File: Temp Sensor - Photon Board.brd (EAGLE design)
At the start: 43.8 x 52.7 mm, 16 parts

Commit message: Added Temp Sensor gerber files.  General cleanup or bck files
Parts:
- U$15: value 50 -> 100
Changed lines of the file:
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@@
 <layer number="21" name="tPlace" color="7" fill="1" visible="yes" active="yes"/>
 <layer number="22" name="bPlace" color="7" fill="1" visible="yes" active="yes"/>
-<layer number="23" name="tOrigins" color="15" fill="1" visible="yes" active="yes"/>
-<layer number="24" name="bOrigins" color="15" fill="1" visible="yes" active="yes"/>
+<layer number="23" name="tOrigins" color="15" fill="1" visible="no" active="yes"/>
+<layer number="24" name="bOrigins" color="15" fill="1" visible="no" active="yes"/>
 <layer number="25" name="tNames" color="7" fill="1" visible="yes" active="yes"/>
 <layer number="26" name="bNames" color="7" fill="1" visible="yes" active="yes"/>
@@
 <text x="60.325" y="99.3775" size="0.508" layer="27" align="center">9V</text>
 <text x="58.42" y="99.3775" size="0.508" layer="27" rot="R180" align="center">GND</text>
-<text x="56.1975" y="93.345" size="0.8128" layer="25" rot="R90">9V Power In</text>
-<text x="63.1825" y="47.9425" size="0.7112" layer="25" rot="R90">Temp Sensor Conn</text>
-<text x="87.3125" y="61.2775" size="1.27" layer="25" rot="R90">Wifi Temperature Sensor Control Board</text>
-<text x="87.3125" y="92.71" size="0.6096" layer="25" rot="R90">v1.0</text>
-<text x="83.185" y="48.5775" size="0.8128" layer="25" rot="R180">http://quiller.io</text>
+<text x="56.1975" y="93.345" size="0.6096" layer="25" rot="R90">9V Power In</text>
+<text x="63.1825" y="47.9425" size="0.6096" layer="25" rot="R90">Temp Sensor Conn</text>
+<text x="87.3125" y="61.2775" size="1" layer="25" rot="R90">Wifi Temperature Sensor Control Board</text>
+<text x="87.6725" y="89.19" size="0.6096" layer="25" rot="R90">v1.0</text>
+<text x="60.285" y="48.6775" size="0.8128" layer="25" rot="R180">http://quiller.io</text>
 <rectangle x1="52.64" y1="70.24" x2="54.64" y2="79.68" layer="16"/>
 <text x="53.3" y="74.82" size="0.3048" layer="27">680</text>
@@
 <element name="U$1" library="myhvac" package="JST_PH-2" value="" x="59.3725" y="92.71" rot="R180"/>
 <element name="D1" library="myhvac" package="LED-RGB-THR" value="LED-RGB-CC-THRU" x="47.38" y="59.37" rot="R90"/>
-<element name="U$15" library="myhvac" package="R0805" value="50" x="57.06" y="64.3" smashed="yes"/>
+<element name="U$15" library="myhvac" package="R0805" value="100" x="57.06" y="64.3" smashed="yes"/>
 <element name="U$16" library="myhvac" package="R0805" value="100" x="57.1" y="61.38" smashed="yes"/>
 <element name="U$17" library="myhvac" package="R0805" value="100" x="57.1" y="58.42" smashed="yes"/>

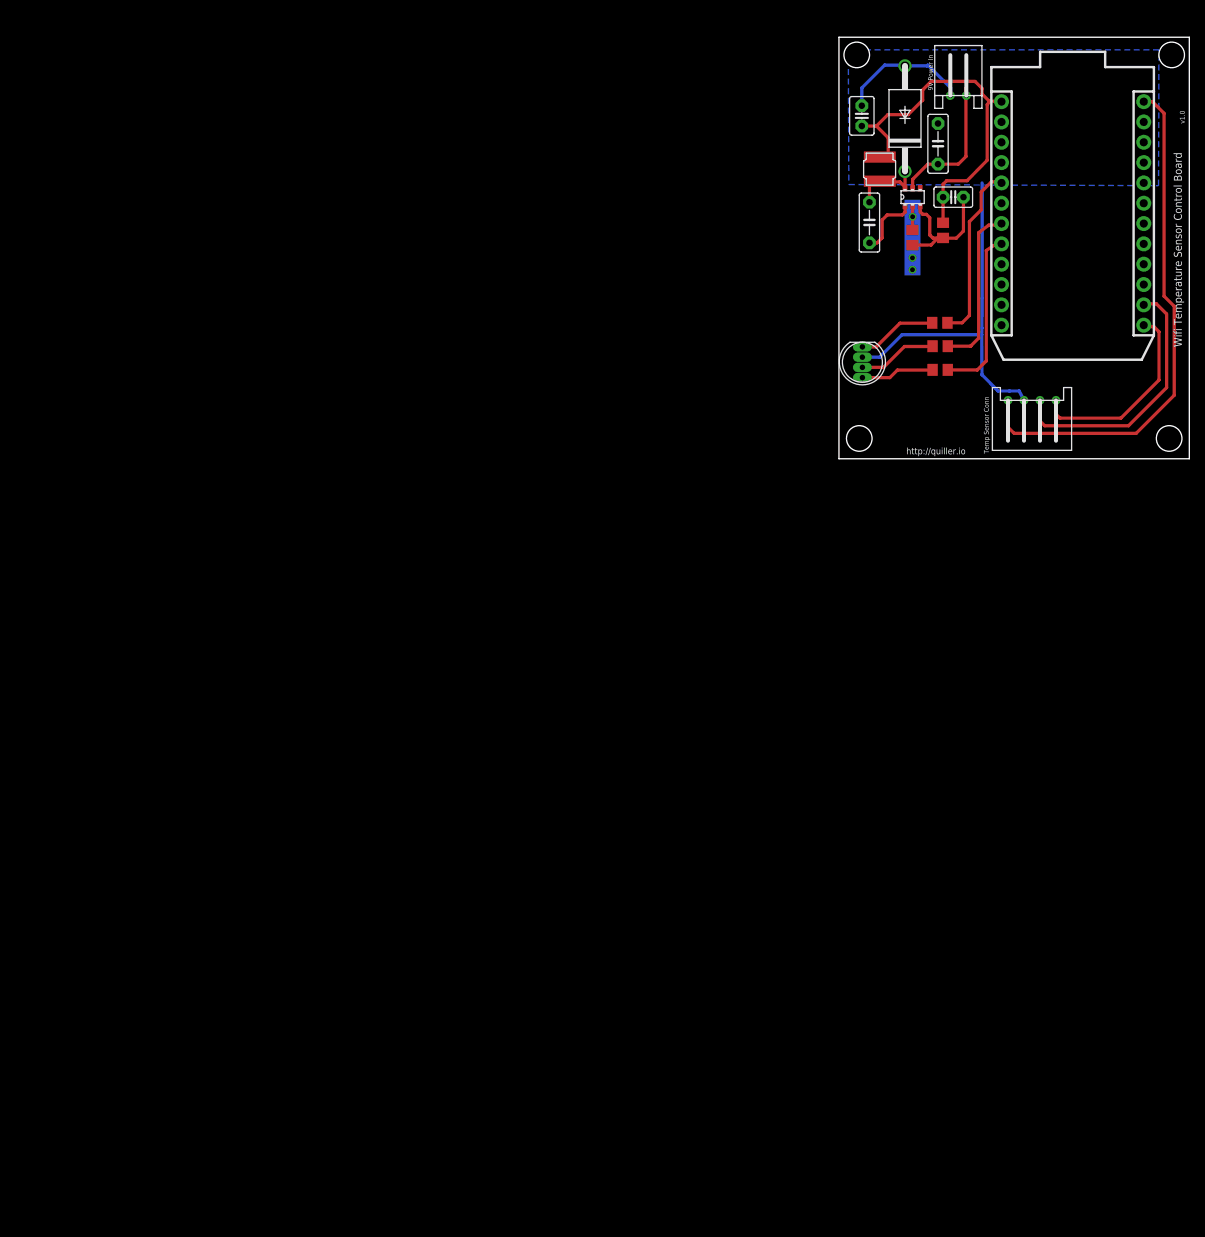
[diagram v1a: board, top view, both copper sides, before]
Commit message: Modified the temp sensor to use a prebuilt power converter
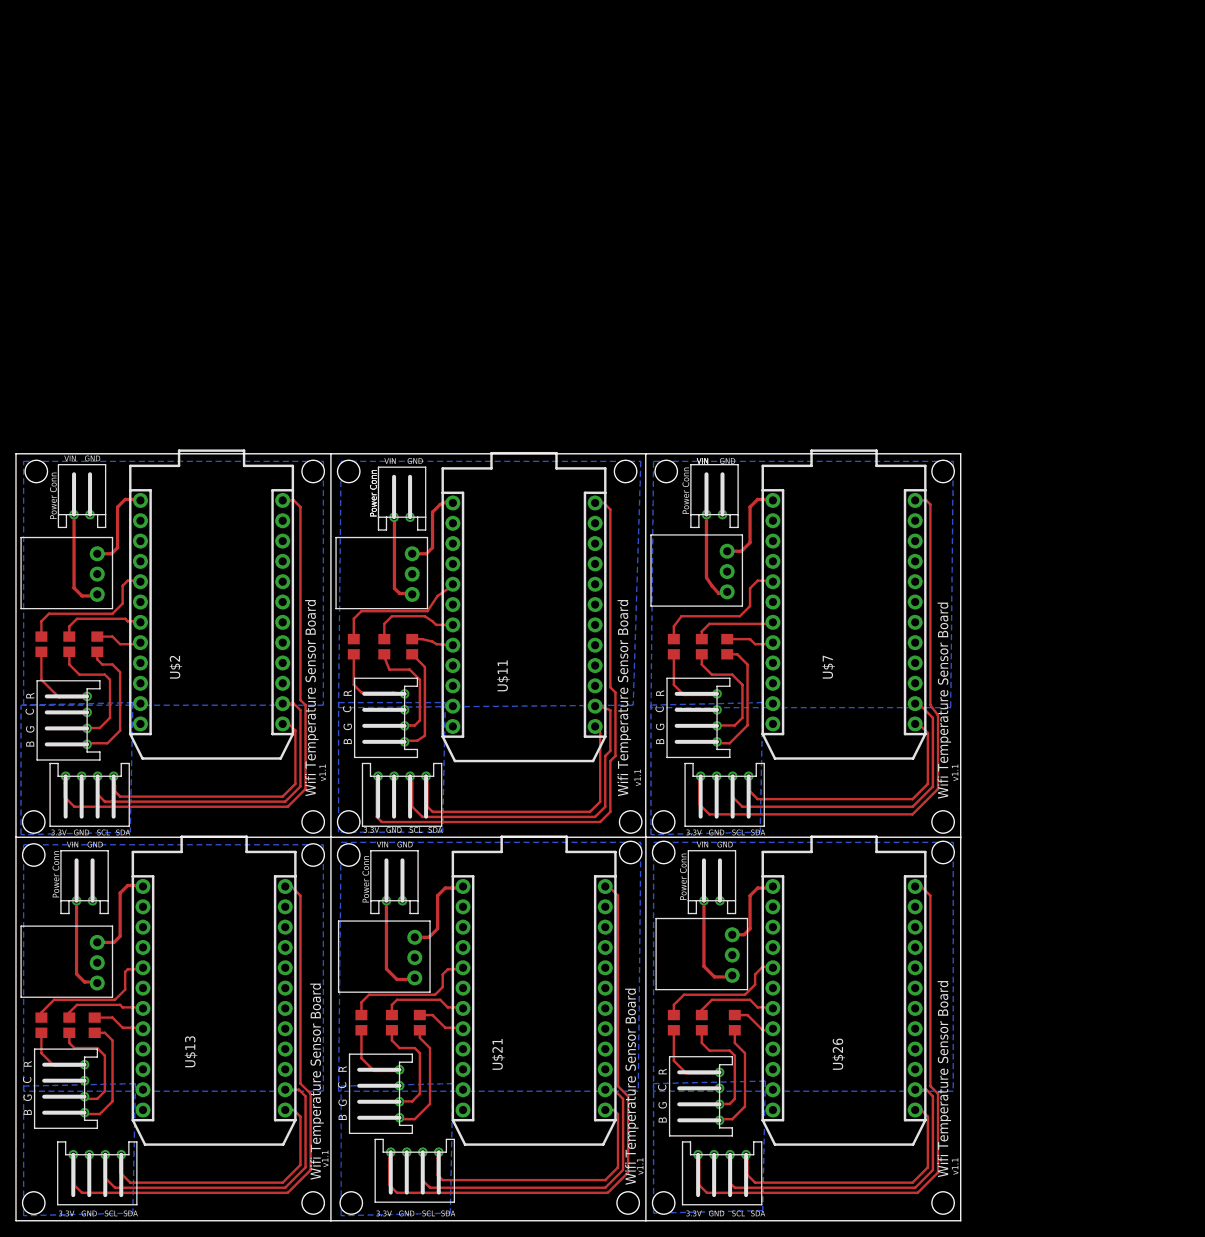
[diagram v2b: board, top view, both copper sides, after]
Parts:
- removed D1: LED-RGB-CC-THRU, myhvac:LED-RGB-THR
- added POWER-CONN-, POWER-CONN-1, POWER-CONN-2, POWER-CONN-3, POWER-CONN-4, POWER-CONN-5: (no value), myhvac:JST_PH-2
- added RGB-LED-CONN-, RGB-LED-CONN-1, RGB-LED-CONN-2, RGB-LED-CONN-3, RGB-LED-CONN-4, RGB-LED-CONN-5, TEMP-SENSOR-CONN-1, TEMP-SENSOR-CONN-2, TEMP-SENSOR-CONN-3, TEMP-SENSOR-CONN-4, TEMP-SENSOR-CONN-5: (no value), myhvac:JST_PH-4
- added U$10, U$14, U$18, U$19, U$22, U$23, U$24, U$27, U$28, U$29, U$9: 100, myhvac:R0805
- added U$20, U$25, U$30: POLOLU_S7V7F5, myhvac:S7V7F5
- added U$21, U$26: Photon w/ Headers, Spark:PHOTON
- U$1: value (none) -> POLOLU_S7V7F5; device myhvac:JST_PH-2 -> myhvac:S7V7F5
- U$12: value 680 -> POLOLU_S7V7F5; device myhvac:R0805 -> myhvac:S7V7F5
- U$13: value 3.9k -> Photon w/ Headers; device myhvac:R0805 -> Spark:PHOTON
- U$2: value 0.1uF -> Photon w/ Headers; device myhvac:C2.5-2 -> Spark:PHOTON
- U$3: value (none) -> 100; device myhvac:SSOP6 -> myhvac:R0805
- U$4: value 15000pF -> 100; device myhvac:C5B2.5 -> myhvac:R0805
- U$5: value 4.7uF -> 100; device myhvac:C5B2.5 -> myhvac:R0805
- U$6: value 10uF -> POLOLU_S7V7F5; device myhvac:C2.5-3 -> myhvac:S7V7F5
- U$7: value RK16 -> Photon w/ Headers; device myhvac:RK_AXIAL -> Spark:PHOTON
- U$8: value NR4018 -> 100; device myhvac:NR_INDUCTOR -> myhvac:R0805
- moved U$13 152.7 mm to (-43.8, -38.4), turned to 0 degrees
- moved U$2 124.5 mm to (-44.1, 9.84), turned to 0 degrees
- moved U$3 122.4 mm to (-55.2, 24.1), turned to 90 degrees
- moved U$5 122.3 mm to (-48.3, 24.1)
- moved U$4 113.1 mm to (-51.8, 24.1)
- moved U$6 111.9 mm to (-48.9, 33.0), turned to 0 degrees
- moved TEMP-SENSOR-CONN- 91.7 mm to (-10.2, 7.62)
- moved U$1 91.2 mm to (-9.53, 33.0), turned to 0 degrees
- moved U$11 85.0 mm to (-5.08, 9.53)
- moved U$15 83.7 mm to (-16.2, 23.8), turned to 90 degrees
- moved U$7 82.0 mm to (34.9, 9.84), turned to 0 degrees
- moved U$16 79.0 mm to (-12.4, 23.8), turned to 90 degrees
- moved U$17 74.5 mm to (-8.89, 23.8), turned to 90 degrees
- moved U$8 65.0 mm to (23.8, 23.8)
- moved U$12 47.9 mm to (29.8, 33.3), turned to 0 degrees
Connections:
- removed net +5V: U$11.1, U$13.1, U$2.2, U$6.1, U$8.P$2
- removed net +9V: U$1.P$1, U$3.P$5, U$5.1
- new net N$10: RGB-LED-CONN-1.P$4, U$5.1
- new net N$14: TEMP-SENSOR-CONN-1.P$1, U$2.24
- new net N$15: TEMP-SENSOR-CONN-1.P$3, U$2.14
- new net N$16: TEMP-SENSOR-CONN-1.P$4, U$2.13
- new net N$17: U$2.5, U$3.2
- new net N$19: U$2.8, U$5.2
- new net N$20: RGB-LED-CONN-1.P$1, U$3.1
- new net N$21: U$2.1, U$6.VOUT
- new net N$22: POWER-CONN-1.P$2, U$6.VIN
- new net N$23: RGB-LED-CONN-2.P$3, U$9.1
- new net N$24: RGB-LED-CONN-2.P$4, U$10.1
- new net N$25: TEMP-SENSOR-CONN-2.P$1, U$7.24
- new net N$26: TEMP-SENSOR-CONN-2.P$3, U$7.14
- new net N$27: TEMP-SENSOR-CONN-2.P$4, U$7.13
- new net N$28: U$7.5, U$8.2
- new net N$29: U$7.7, U$9.2
- new net N$30: U$10.2, U$7.8
- new net N$31: RGB-LED-CONN-2.P$1, U$8.1
- new net N$32: U$12.VOUT, U$7.1
- new net N$33: POWER-CONN-2.P$2, U$12.VIN
- new net N$34: RGB-LED-CONN-3.P$3, U$18.1
- new net N$35: RGB-LED-CONN-3.P$4, U$19.1
- new net N$36: TEMP-SENSOR-CONN-3.P$1, U$13.24
- new net N$37: TEMP-SENSOR-CONN-3.P$3, U$13.14
- new net N$38: TEMP-SENSOR-CONN-3.P$4, U$13.13
- new net N$39: U$13.5, U$14.2
- new net N$40: U$13.7, U$18.2
- new net N$41: U$13.8, U$19.2
- new net N$42: RGB-LED-CONN-3.P$1, U$14.1
- new net N$43: U$13.1, U$20.VOUT
- new net N$44: POWER-CONN-3.P$2, U$20.VIN
- new net N$45: RGB-LED-CONN-4.P$3, U$23.1
- new net N$46: RGB-LED-CONN-4.P$4, U$24.1
- new net N$47: TEMP-SENSOR-CONN-4.P$1, U$21.24
- new net N$48: TEMP-SENSOR-CONN-4.P$3, U$21.14
- new net N$49: TEMP-SENSOR-CONN-4.P$4, U$21.13
- new net N$50: U$21.5, U$22.2
- new net N$51: U$21.7, U$23.2
- new net N$52: U$21.8, U$24.2
- new net N$53: RGB-LED-CONN-4.P$1, U$22.1
- new net N$54: U$21.1, U$25.VOUT
- new net N$55: POWER-CONN-4.P$2, U$25.VIN
- new net N$56: RGB-LED-CONN-5.P$3, U$28.1
- new net N$57: RGB-LED-CONN-5.P$4, U$29.1
- new net N$58: TEMP-SENSOR-CONN-5.P$1, U$26.24
- new net N$59: TEMP-SENSOR-CONN-5.P$3, U$26.14
- new net N$60: TEMP-SENSOR-CONN-5.P$4, U$26.13
- new net N$61: U$26.5, U$27.2
- new net N$62: U$26.7, U$28.2
- new net N$63: U$26.8, U$29.2
- new net N$64: RGB-LED-CONN-5.P$1, U$27.1
- new net N$65: U$26.1, U$30.VOUT
- new net N$66: POWER-CONN-5.P$2, U$30.VIN
- net GND: now also POWER-CONN-.P$1, POWER-CONN-1.P$1, POWER-CONN-2.P$1, POWER-CONN-3.P$1, POWER-CONN-4.P$1, POWER-CONN-5.P$1, RGB-LED-CONN-.P$2, RGB-LED-CONN-1.P$2, RGB-LED-CONN-2.P$2, RGB-LED-CONN-3.P$2, RGB-LED-CONN-4.P$2, RGB-LED-CONN-5.P$2, TEMP-SENSOR-CONN-1.P$2, TEMP-SENSOR-CONN-2.P$2, TEMP-SENSOR-CONN-3.P$2, TEMP-SENSOR-CONN-4.P$2, TEMP-SENSOR-CONN-5.P$2, U$1.GND, U$12.GND, U$13.2, U$13.21, U$2.2, U$2.21, U$20.GND, U$21.2, U$21.21, U$25.GND, U$26.2, U$26.21, U$30.GND, U$6.GND, U$7.2, U$7.21; no longer D1.P$2, U$1.P$2, U$5.2, U$6.2, U$7.A
- net N$13: now also RGB-LED-CONN-.P$1; no longer D1.P$1
- net N$18: now also U$2.7, U$4.2; no longer U$12.1, U$3.P$2
- net N$2: now also RGB-LED-CONN-.P$3; no longer D1.P$3
- net N$3: now also RGB-LED-CONN-.P$4; no longer D1.P$4
- net N$4: now also U$1.VOUT, U$11.1; no longer U$3.P$1, U$4.1
- net N$5: now also POWER-CONN-.P$2, U$1.VIN; no longer U$3.P$6, U$4.2, U$7.C, U$8.P$1
- net N$6: now also RGB-LED-CONN-1.P$3, U$4.1; no longer U$12.2, U$13.2, U$2.1, U$3.P$3
- net VBAT: now also U$13.22, U$2.22, U$21.22, U$26.22, U$7.22
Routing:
- net N$25: track 0.00 -> 73.2 mm
- net N$47: track 0.00 -> 72.6 mm
- net N$58: track 0.00 -> 72.5 mm
- net N$14: track 0.00 -> 72.2 mm
- net N$36: track 0.00 -> 72.2 mm
- net GND: track 63.7 -> 0.00 mm
- net +5V: track 45.4 -> 0.00 mm
- net N$59: track 0.00 -> 41.9 mm
- net N$48: track 0.00 -> 41.5 mm
- net N$37: track 0.00 -> 41.3 mm
- net N$15: track 0.00 -> 40.9 mm, vias 1 -> 0
- net N$26: track 0.00 -> 40.8 mm
- net N$49: track 0.00 -> 34.8 mm
- net N$60: track 0.00 -> 34.6 mm
- net N$38: track 0.00 -> 34.6 mm
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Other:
- board size 43.8 x 52.7 mm -> 118.1 x 95.9 mm
- board text added: "B"
- board text added: "C"
- board text added: "G"
- board text added: "Power Conn"
- board text added: "R"
- board text added: "VIN"
- board text added: "Wifi Temperature Sensor Board"
- board text added: "v1.1"
- board text removed: "100"
- board text removed: "3.9k"
- board text removed: "50"
- board text removed: "680"
- board text removed: "9V"
- board text removed: "9V Power In"
- board text removed: "BD9G101G‑TR"
- board text removed: "NR4018T6R8M"
- board text removed: "Temp Sensor Conn"
- board text removed: "Wifi Temperature Sensor Control Board"
- board text removed: "http://quiller.io"
- board text removed: "v1.0"
